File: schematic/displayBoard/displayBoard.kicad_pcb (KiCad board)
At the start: 2 copper layers, 55 x 55 mm, 30 parts, among them IC1 4028D, T1 MMBTA42, T10 MMBTA42, T2 MMBTA42, T3 MMBTA42, T4 MMBTA42, T5 MMBTA42, T6 MMBTA42, T7 MMBTA42, T8 MMBTA42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

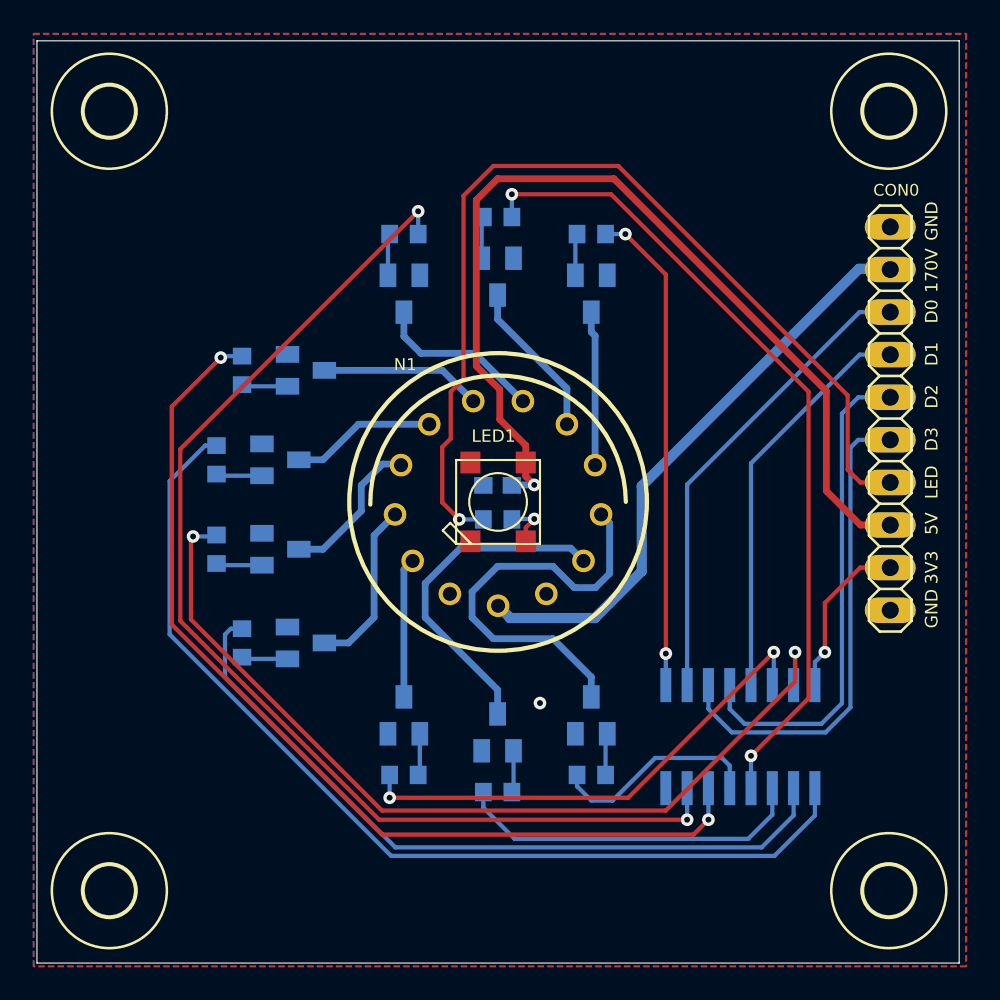
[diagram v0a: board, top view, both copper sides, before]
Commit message: Re-wire control display with KiCad components
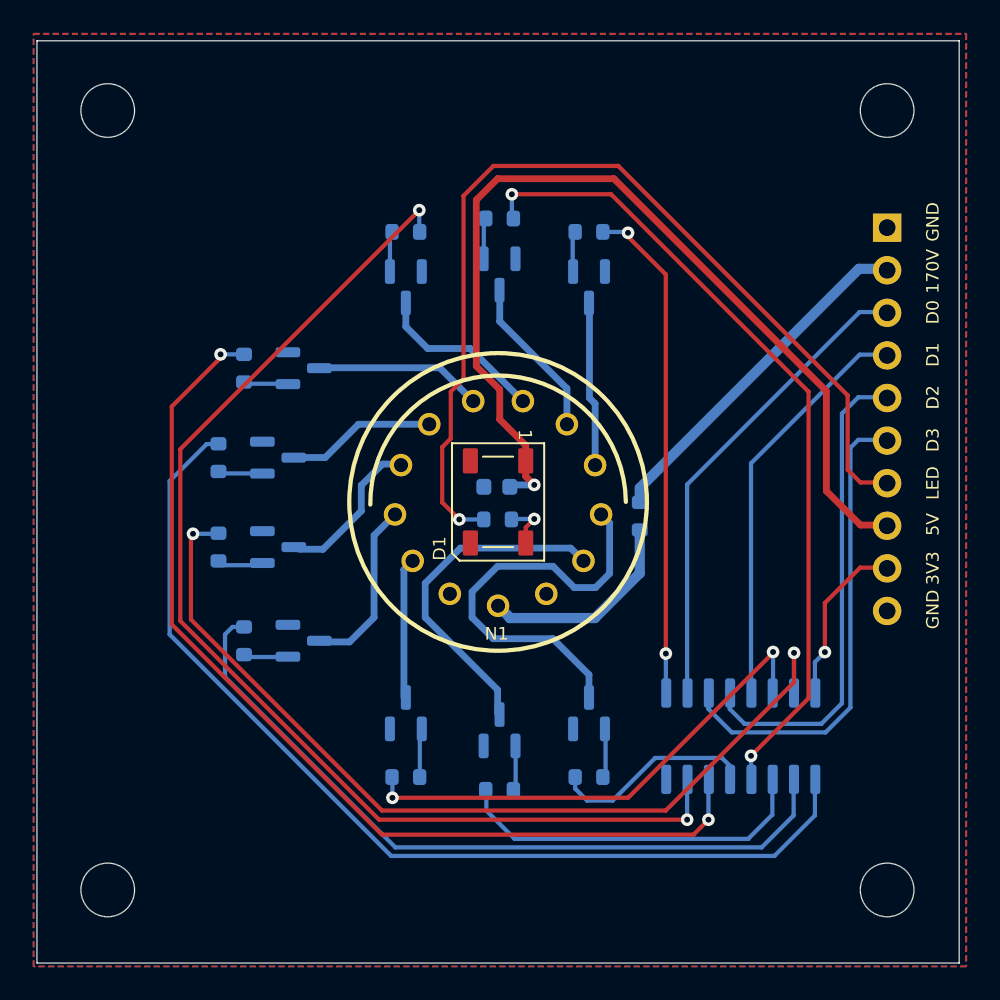
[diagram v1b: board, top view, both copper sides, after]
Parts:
- removed CON0: , displayBoard:1X10_325
- removed IC1: 4028D, displayBoard:SO16_80
- removed LED1: WS2812B_5050N, displayBoard:WS2812B-NARROW
- removed T1, T10, T2, T3, T4, T5, T6, T7, T8, T9: MMBTA42, displayBoard:SOT23-BEC_402
- added D1: WS2812B, LED_SMD:LED_WS2812B_PLCC4_5.0x5.0mm_P3.2mm, F.Cu at (148.5, 105.0)
- added J1: Conn_01x10_Pin, Connector_PinHeader_2.54mm:PinHeader_1x10_P2.54mm_Vertical, B.Cu at (171.7, 88.6)
- added Q1: MMBTA42, Package_TO_SOT_SMD:SOT-23, B.Cu at (148.6, 118.6)
- added Q10: MMBTA42, Package_TO_SOT_SMD:SOT-23, B.Cu at (153.9, 117.6)
- added Q2: MMBTA42, Package_TO_SOT_SMD:SOT-23, B.Cu at (136.9, 97.0)
- added Q3: MMBTA42, Package_TO_SOT_SMD:SOT-23, B.Cu at (143.0, 117.6)
- added Q4: MMBTA42, Package_TO_SOT_SMD:SOT-23, B.Cu at (143.0, 92.2)
- added Q5: MMBTA42, Package_TO_SOT_SMD:SOT-23, B.Cu at (136.9, 113.3)
- added Q6: MMBTA42, Package_TO_SOT_SMD:SOT-23, B.Cu at (148.6, 91.4)
- added Q7: MMBTA42, Package_TO_SOT_SMD:SOT-23, B.Cu at (135.4, 107.7)
- added Q8: MMBTA42, Package_TO_SOT_SMD:SOT-23, B.Cu at (153.9, 92.2)
- added Q9: MMBTA42, Package_TO_SOT_SMD:SOT-23, B.Cu at (135.4, 102.4)
- added R12: 18k, Resistor_SMD:R_0603_1608Metric, B.Cu at (157.0, 105.9)
- added U1: 4028, Package_SO:SO-16_3.9x9.9mm_P1.27mm, B.Cu at (163.0, 119.0)
- C1: footprint displayBoard:C0603_348 -> Capacitor_SMD:C_0603_1608Metric
- H1, H2, H3, H4: value MOUNT-HOLE3.0 -> ~; footprint displayBoard:3,0_237 -> MountingHole:MountingHole_3.2mm_M3
- R1, R10, R11, R2, R3, R4, R5, R6, R7, R8, R9: footprint displayBoard:R0603_348 -> Resistor_SMD:R_0603_1608Metric
- moved H1 65.8 mm to (125.2, 128.1)
- moved H3 65.7 mm to (171.7, 81.7)
- moved R2 26.1 mm to (133.3, 97.0), turned to -90 degrees
- moved R9 25.9 mm to (131.8, 102.4), turned to -90 degrees
- moved R4 22.0 mm to (143.0, 88.9), turned to 180 degrees
- moved R7 21.7 mm to (131.8, 107.7), turned to -90 degrees
- moved R6 17.8 mm to (148.6, 88.1), turned to 180 degrees
- moved R3 12.6 mm to (143.0, 121.4), turned to 0 degrees
- moved R5 10.9 mm to (133.3, 113.3)
- moved R8 5.52 mm to (153.9, 88.9)
- moved R10 0.19 mm to (153.9, 121.4)
- moved R1 0.17 mm to (148.6, 122.2)
- moved H2 0.11 mm to (125.2, 81.7)
- moved H4 0.11 mm to (171.7, 128.1)
- moved C1 0.10 mm to (148.4, 104.1), turned to 180 degrees
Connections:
- C1 pad 1: GND -> +5V
- C1 pad 2: +5V -> GND
- N1 pad 0: NIXIE0 -> /NIXIE0
- N1 pad 1: NIXIE1 -> /NIXIE1
- N1 pad 2: NIXIE2 -> /NIXIE2
- N1 pad 3: NIXIE3 -> /NIXIE3
- N1 pad 4: NIXIE4 -> /NIXIE4
- N1 pad 5: NIXIE5 -> /NIXIE5
- N1 pad 6: NIXIE6 -> /NIXIE6
- N1 pad 7: NIXIE7 -> /NIXIE7
- N1 pad 8: NIXIE8 -> /NIXIE8
- N1 pad 9: NIXIE9 -> /NIXIE9
- N1 pad A: VCC -> Net-(N1-PadA)
- N1 pad LHDP: (no net) -> unconnected-(N1-PadLHDP)
- N1 pad RHDP: (no net) -> unconnected-(N1-PadRHDP)
- R1 pad 1: DIG0 -> /DIG0
- R10 pad 1: DIG9 -> /DIG9
- R11 pad 1: LED -> /LED
- R2 pad 1: DIG1 -> /DIG5
- R3 pad 1: DIG2 -> /DIG1
- R4 pad 1: DIG3 -> /DIG6
- R5 pad 1: DIG4 -> /DIG2
- R6 pad 1: DIG5 -> /DIG7
- R7 pad 1: DIG6 -> /DIG3
- R8 pad 1: DIG7 -> /DIG8
- R9 pad 1: DIG8 -> /DIG4
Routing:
- net /DIG6: track 0.00 -> 68.9 mm, vias 0 -> 2
- net DIG6: track 68.7 -> 0.00 mm, vias 2 -> 0
- net /DIG4: track 0.00 -> 59.5 mm
- net DIG4: track 59.4 -> 0.00 mm
- net LED: track 58.3 -> 0.00 mm, vias 1 -> 0
- net /LED: track 0.00 -> 58.3 mm, vias 0 -> 1
- net /DIG5: track 0.00 -> 58.1 mm, vias 0 -> 2
- net DIG5: track 57.9 -> 0.00 mm, vias 2 -> 0
- net /DIG3: track 0.00 -> 54.1 mm, vias 0 -> 2
- net DIG3: track 54.1 -> 0.00 mm, vias 2 -> 0
- net DIG7: track 49.0 -> 0.00 mm, vias 2 -> 0
- net /DIG7: track 0.00 -> 49.0 mm, vias 0 -> 2
- net /DIG2: track 0.00 -> 44.3 mm
- net DIG2: track 44.2 -> 0.00 mm
- net DIG1: track 29.9 -> 0.00 mm, vias 2 -> 0
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
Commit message: Fix weird behaviour of the LED by adding a level shifter to DIN pin
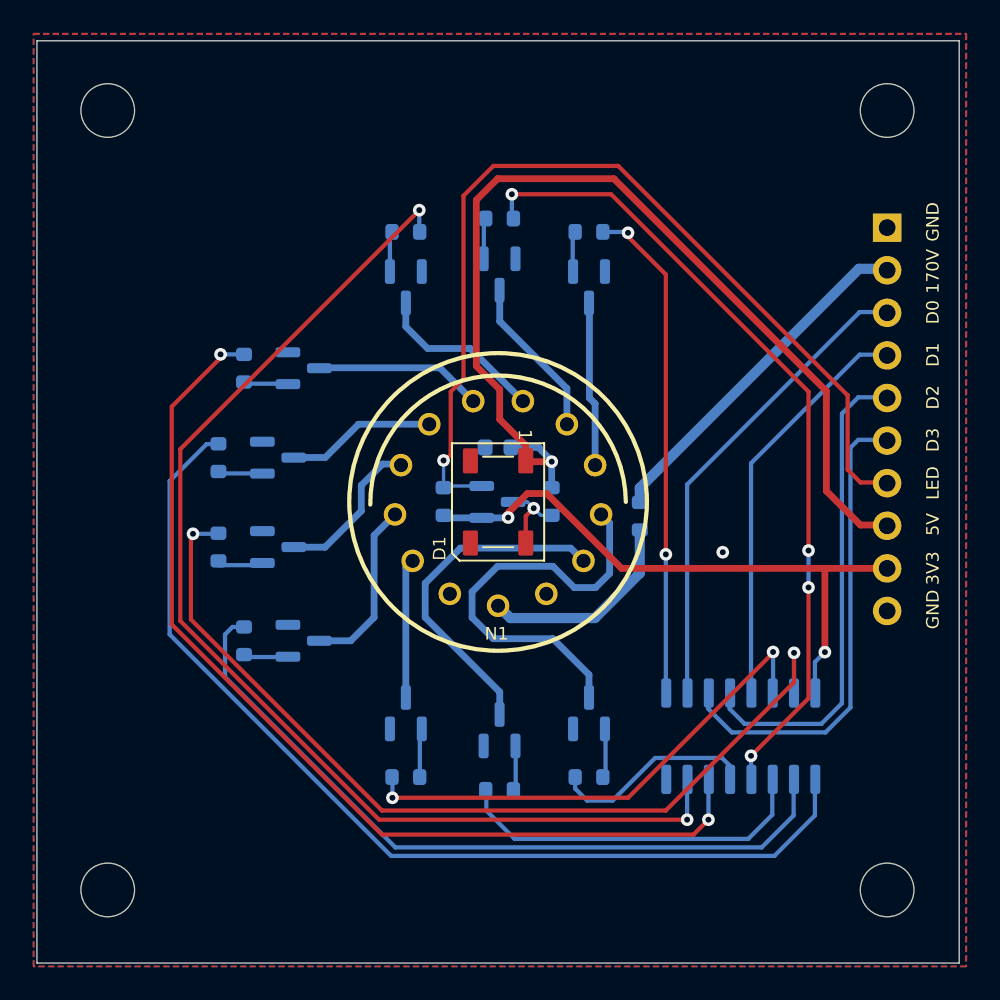
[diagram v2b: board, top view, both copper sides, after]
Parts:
- added Q11: BSS123, Package_TO_SOT_SMD:SOT-23, B.Cu at (148.5, 105.0)
- added R13: 10k, Resistor_SMD:R_0603_1608Metric, B.Cu at (151.7, 105.0)
- R11: value 470 -> 10k
- moved R11 3.39 mm to (145.3, 105.0), turned to -90 degrees
- moved C1 2.35 mm to (148.5, 101.8)
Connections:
- R11 pad 2: Net-(D1-DIN) -> +3V3
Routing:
- net +3V3: track 9.92 -> 36.3 mm, vias 1 -> 2
- net +5V: track 57.0 -> 59.6 mm
- net Net-(D1-DIN): track 2.89 -> 4.85 mm
- net /LED: track 58.3 -> 56.8 mm
- net GND: vias 0 -> 1
- net /DIG7: vias 2 -> 4

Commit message: Match via sizes between two PCBs
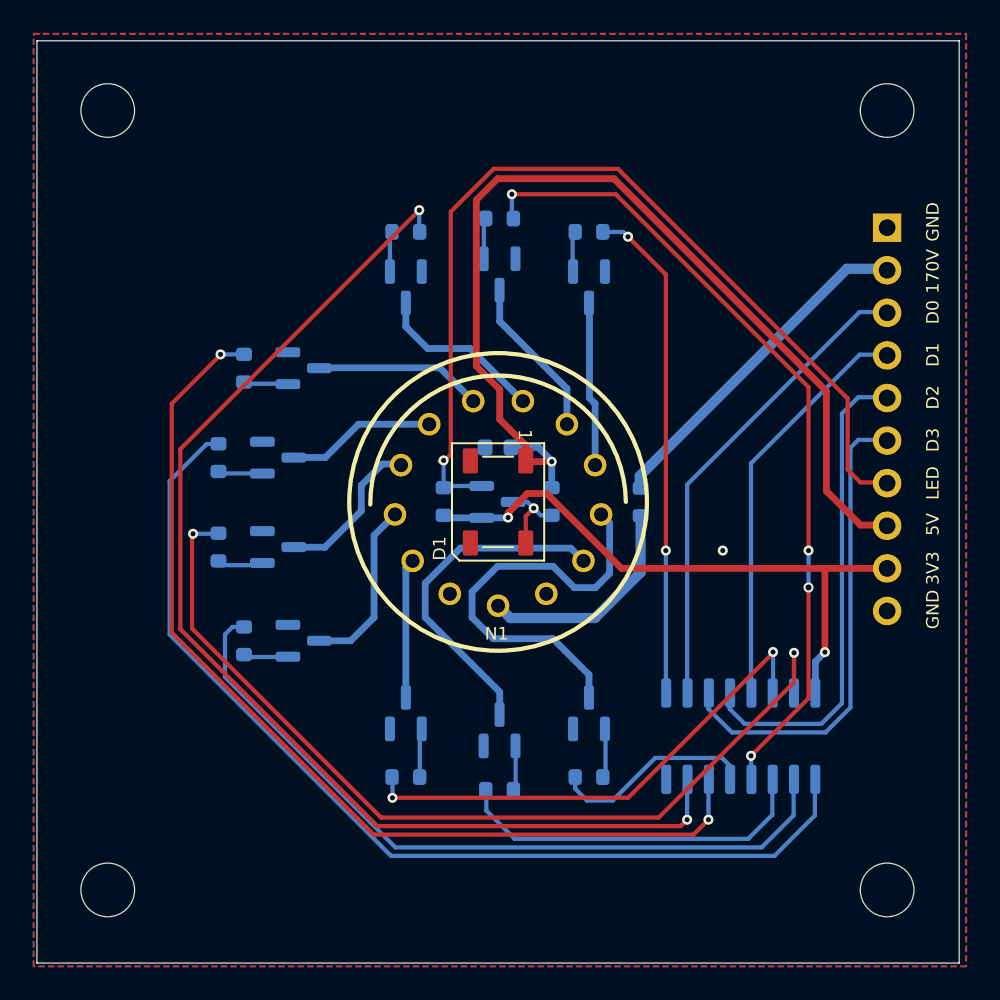
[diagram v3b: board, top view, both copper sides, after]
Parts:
- moved R12 0.85 mm to (157.0, 105.0)
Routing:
- net /DIG6: track 68.9 -> 69.5 mm
- net /DIG3: track 54.1 -> 54.7 mm
